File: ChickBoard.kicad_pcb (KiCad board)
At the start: 2 copper layers, 40 x 30 mm, 12 parts, among them CON1 AVR-ISP-6, J1 Screw_Terminal_1x04, J2 CONN_01X02, J3 CONN_01X02, J4 CONN_01X02, Q1 Q_NMOS_DGS, Q2 Q_PMOS_DGS, U1 ATMEGA328-AU, U2 SN65HVD485E, U3 RFID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

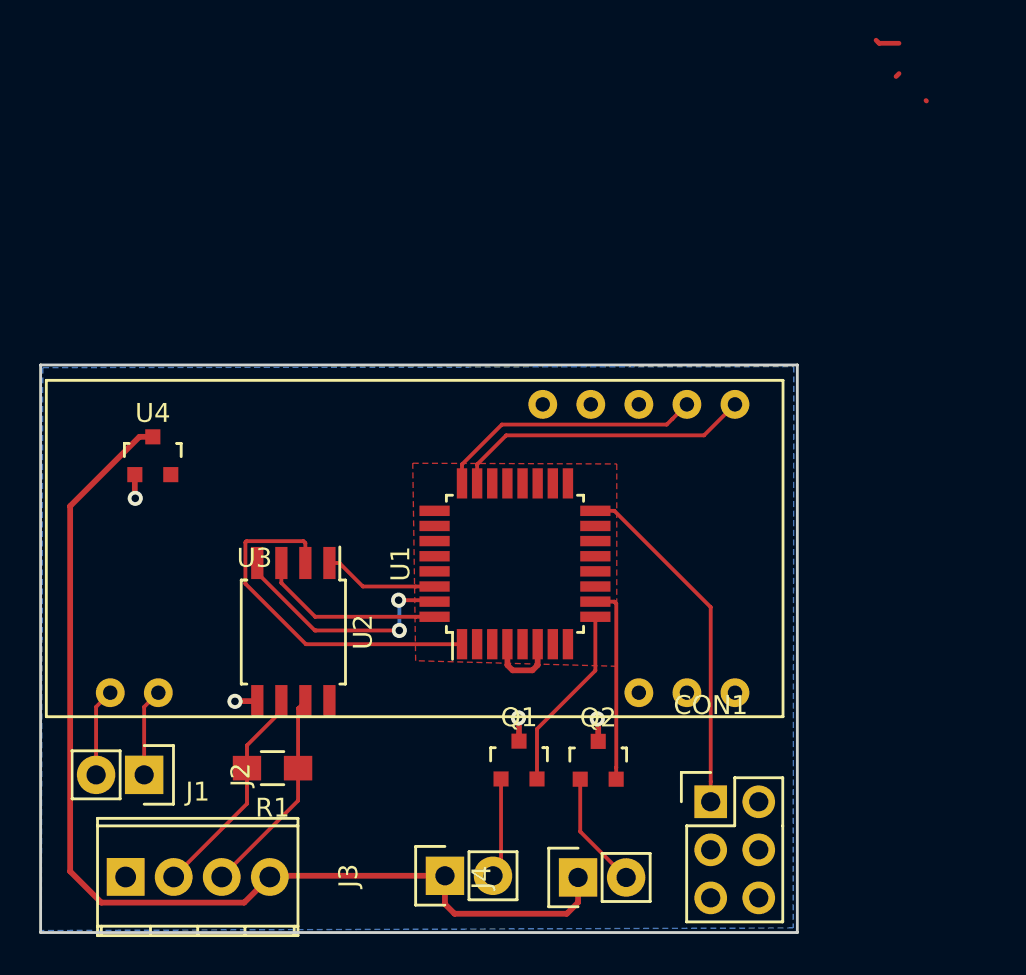
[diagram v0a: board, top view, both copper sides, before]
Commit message: Switched to SAMD20 mcu
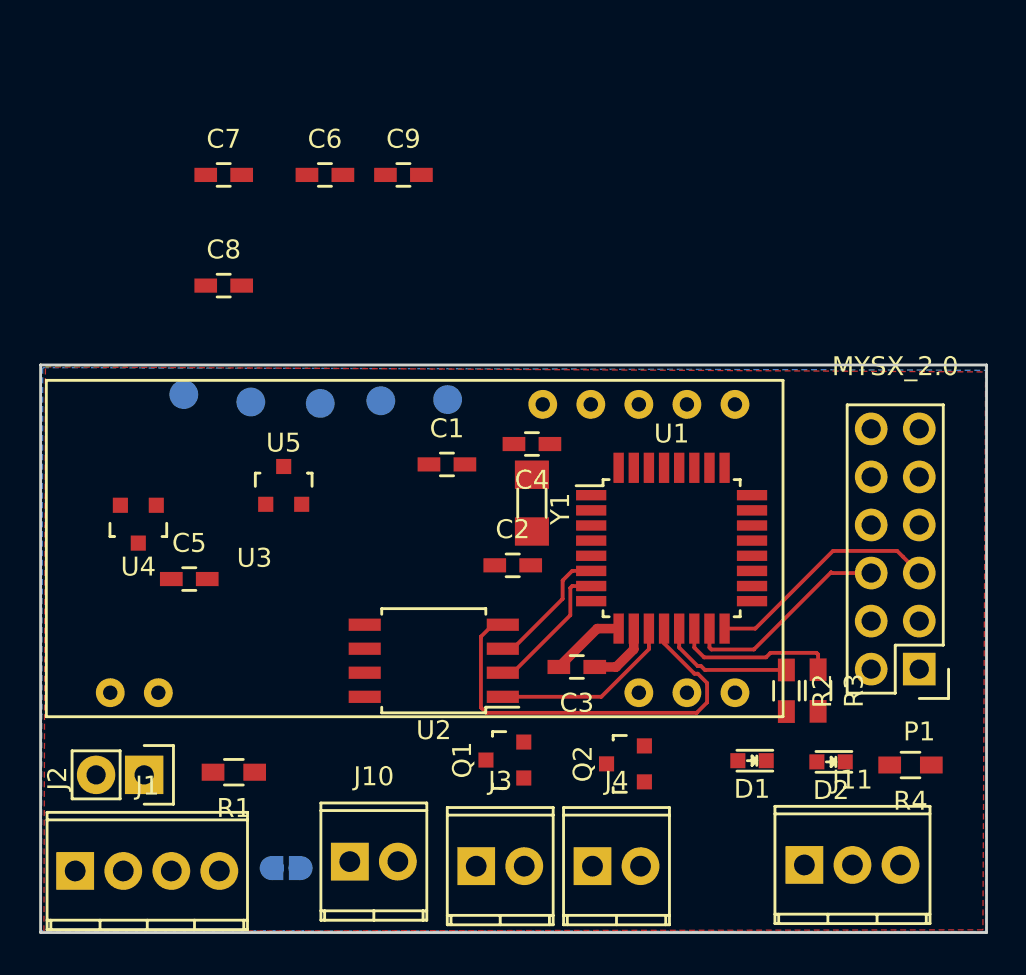
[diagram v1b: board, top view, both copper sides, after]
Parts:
- removed CON1: AVR-ISP-6, Pin_Headers:Pin_Header_Straight_2x03
- added C1: 4.7pF, Capacitors_SMD:C_0603_HandSoldering, F.Cu at (121.5, 105.3)
- added C2: 4.7pF, Capacitors_SMD:C_0603_HandSoldering, F.Cu at (125.0, 110.6)
- added C3: 100nF, Capacitors_SMD:C_0603_HandSoldering, F.Cu at (128.3, 116.0)
- added C4: 100nF, Capacitors_SMD:C_0603_HandSoldering, F.Cu at (126.0, 104.2)
- added C5: 100nF, Capacitors_SMD:C_0603_HandSoldering, F.Cu at (107.9, 111.3)
- added C6: CP, Capacitors_SMD:C_0603_HandSoldering, F.Cu at (115.0, 90.0)
- added C7: C_Small, Capacitors_SMD:C_0603_HandSoldering, F.Cu at (109.7, 90.0)
- added C8: C_Small, Capacitors_SMD:C_0603_HandSoldering, F.Cu at (109.7, 95.8)
- added C9: CP, Capacitors_SMD:C_0603_HandSoldering, F.Cu at (119.2, 90.0)
- added D1: LED, LEDs:LED-0603, F.Cu at (137.6, 120.9)
- added D2: LED, LEDs:LED-0603, F.Cu at (141.8, 121.0)
- added J10: Led PWR in, Terminal_Blocks:TerminalBlock_Pheonix_MPT-2.54mm_2pol, F.Cu at (116.3, 126.3)
- added J11: CONN_01X03, Terminal_Blocks:TerminalBlock_Pheonix_MPT-2.54mm_3pol, F.Cu at (140.4, 126.4)
- added J5: TEST_1P, Measurement_Points:Measurement_Point_Round-SMD-Pad_Small, B.Cu at (121.5, 101.8)
- added J6: TEST_1P, Measurement_Points:Measurement_Point_Round-SMD-Pad_Small, B.Cu at (107.6, 101.6)
- added J7: TEST_1P, Measurement_Points:Measurement_Point_Round-SMD-Pad_Small, B.Cu at (114.8, 102.0)
- added J8: TEST_1P, Measurement_Points:Measurement_Point_Round-SMD-Pad_Small, B.Cu at (118.0, 101.9)
- added J9: TEST_1P, Measurement_Points:Measurement_Point_Round-SMD-Pad_Small, B.Cu at (111.1, 102.0)
- added JP1: Jumper, mysensors_obscurities:2_pin_solder_jumper_smd, B.Cu at (113.0, 126.6)
- added P1: MYSX_2.0, mysensors_connectors:MYSX_2.2, F.Cu at (146.4, 116.1)
- added R2: R, Resistors_SMD:R_0603_HandSoldering, F.Cu at (139.4, 117.2)
- added R3: R, Resistors_SMD:R_0603_HandSoldering, F.Cu at (141.1, 117.2)
- added R4: R, Resistors_SMD:R_0603_HandSoldering, F.Cu at (146.0, 121.1)
- added U5: AMS1117, TO_SOT_Packages_SMD:SOT-23, F.Cu at (112.8, 106.4)
- added Y1: 32Khz, mysensors_obscurities:XTAL_3.2x1.5mm, F.Cu at (126.0, 107.3)
- J1: value Screw_Terminal_1x04 -> rs485_bus
- J3: value CONN_01X02 -> LED ch1; footprint Pin_Headers:Pin_Header_Straight_1x02 -> Terminal_Blocks:TerminalBlock_Pheonix_MPT-2.54mm_2pol
- J4: value CONN_01X02 -> LED ch2; footprint Pin_Headers:Pin_Header_Straight_1x02 -> Terminal_Blocks:TerminalBlock_Pheonix_MPT-2.54mm_2pol
- R1: value 75R -> R_Small; footprint Resistors_SMD:R_0805_HandSoldering -> Resistors_SMD:R_0603_HandSoldering
- U1: value ATMEGA328-AU -> ATSAMD21E
- moved U1 8.32 mm to (133.4, 109.7), turned to 0 degrees
- moved U2 7.58 mm to (120.8, 115.6), turned to 180 degrees
- moved U4 3.70 mm to (105.2, 108.4), turned to 180 degrees
- moved J1 2.69 mm to (101.8, 126.7)
- moved R1 2.06 mm to (110.2, 121.5)
- moved J3 1.73 mm to (123.0, 126.5), turned to 0 degrees
- moved Q2 1.45 mm to (130.9, 121.1), turned to 90 degrees
- moved J4 0.97 mm to (129.2, 126.5), turned to 0 degrees
- moved Q1 0.75 mm to (124.5, 120.9), turned to 90 degrees
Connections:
- J3 pad 1: +12V -> Net-(J10-Pad1)
- J4 pad 1: +12V -> Net-(J10-Pad1)
- Q1 pad 2: Net-(Q1-Pad2) -> /PWM1
- Q2 pad 2: Net-(Q2-Pad2) -> /PWM2
- U1 pad 1: Net-(U1-Pad1) -> Net-(C1-Pad2)
- U1 pad 10: Net-(Q2-Pad2) -> GND
- U1 pad 11: Net-(U1-Pad11) -> /485_RX
- U1 pad 12: Net-(U1-Pad12) -> /485_TX
- U1 pad 13: Net-(U1-Pad13) -> /LED1
- U1 pad 14: Net-(U1-Pad14) -> /LED2
- U1 pad 15: Net-(CON1-Pad4) -> /D2_DTM
- U1 pad 16: Net-(CON1-Pad1) -> /D1_DFM
- U1 pad 18: +5V -> Net-(U1-Pad18)
- U1 pad 21: GND -> /RF_RX
- U1 pad 22: Net-(U1-Pad22) -> /RF_TX
- U1 pad 23: /RF_TX -> /1_wire
- U1 pad 24: /RF_RX -> Net-(U1-Pad24)
- U1 pad 28: Net-(U1-Pad28) -> GND
- U1 pad 3: GND -> Net-(U1-Pad3)
- U1 pad 30: Net-(U1-Pad30) -> +3V3
- U1 pad 31: Net-(U1-Pad31) -> /SWCLK
- U1 pad 32: Net-(U1-Pad32) -> /SWDIO
- U1 pad 4: +5V -> Net-(U1-Pad4)
- U1 pad 5: GND -> Net-(U1-Pad5)
- U1 pad 6: +5V -> /485_TXE
- U1 pad 7: Net-(U1-Pad7) -> /485_RXE
- U1 pad 9: Net-(Q1-Pad2) -> +3V3
- U2 pad 1: Net-(U1-Pad30) -> /485_RX
- U2 pad 2: Net-(U1-Pad1) -> /485_RXE
- U2 pad 3: Net-(U1-Pad32) -> /485_TXE
- U2 pad 4: Net-(U1-Pad31) -> /485_TX
- U2 pad 8: +5V -> +3V3
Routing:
- net +12V: track 56.8 -> 0.00 mm
- net /485_TX: track 0.00 -> 22.4 mm
- net Net-(U1-Pad1): track 19.3 -> 0.00 mm
- net Net-(CON1-Pad1): track 18.5 -> 0.00 mm
- net /RF_TX: track 15.9 -> 0.00 mm
- net /RF_RX: track 14.2 -> 0.00 mm
- net Net-(U1-Pad31): track 12.8 -> 0.00 mm, vias 2 -> 0
- net /D1_DFM: track 0.00 -> 12.5 mm
- net Net-(J1-Pad2): track 11.7 -> 0.00 mm
- net /D2_DTM: track 0.00 -> 11.3 mm
- net Net-(J1-Pad3): track 11.1 -> 0.00 mm
- net Net-(Q2-Pad2): track 10.4 -> 0.00 mm
- net Net-(U1-Pad32): track 9.89 -> 0.00 mm
- net /485_RX: track 0.00 -> 9.85 mm
- net Net-(Q1-Pad2): track 9.85 -> 0.00 mm
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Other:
- board size 40 x 30 mm -> 50 x 30 mm
- net class POWER: trace_width 0.3048 -> 0.508
